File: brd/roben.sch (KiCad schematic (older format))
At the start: 44 parts, among them J1 POWER IN, J10 1+, J11 1-, J12 2-, J13 2+, J2 +V, J3 GND, J4 +V, J5 GND, J6 A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

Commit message: chg: dev: añadidas referencias datasheet y BOM
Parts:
- C1: Vendor (none) -> 81-GRM219R6YA475M3D3
- C2, C4: Vendor (none) -> 843-0805J0500104KJT
- C3: Vendor (none) -> 77-VJ0805Y822KXBPBC
- C5: Vendor (none) -> 77-VJ0805A391KXACBC
- C6: Vendor (none) -> 603-CC805DRNPO9BN7R0
- C7: Vendor (none) -> 81-GRM219R61C226ME5L
- C8: Vendor (none) -> 140-VE101M1CTR0605
- D1, D2, D7: Vendor (none) -> 621-B340-F
- D3, D4, D5, D6: Vendor (none) -> 821-BZT52B5V1
- D8: Vendor (none) -> 720-LOR976-PS-1
- F1: Vendor (none) -> 530-0ZCF0200FF2C
- J1: Vendor (none) -> 651-1985946
- L1: Vendor (none) -> 652-SRN8040-8R2Y
- R10, R6, R7, R8, R9: Vendor (none) -> 71-CRCW0805-220-E3
- R2: Vendor (none) -> 71-CRCW0805-1.0M-E3
- R3: Vendor (none) -> 71-CRCW0805-10K-E3
- R4: Vendor (none) -> 71-CRCW0805-2.0K-E3
- R5: Vendor (none) -> 71-CRCW0805-63.4K-E3
- U1: Vendor (none) -> 595-TPS54232DR
- U2: Vendor (none) -> 595-SN754410NE
- U3: Vendor (none) -> 992-ARD-NANO30
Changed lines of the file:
@@
 F 1 "TPS54232" H 3350 1875 50  0000 C CNN
 F 2 "Housings_SOIC:SOIC-8_3.9x4.9mm_Pitch1.27mm" H 3350 1775 50  0001 C CNN
-F 3 "DOCUMENTATION" H 3350 1775 50  0001 C CNN
+F 3 "http://www.ti.com/lit/ds/symlink/tps54232.pdf" H 3350 1775 50  0001 C CNN
+F 4 "595-TPS54232DR" H 3350 1775 60  0001 C CNN "Vendor"
 	1    3350 1775
 	1    0    0    -1
@@
 F 1 "SN754410N" H 3525 4725 50  0000 C CNN
 F 2 "Housings_DIP:DIP-16__300_ELL" H 3525 4625 50  0001 C CNN
-F 3 "DOCUMENTATION" H 3525 4625 50  0001 C CNN
+F 3 "http://www.ti.com/lit/ds/symlink/sn754410.pdf" H 3525 4625 50  0001 C CNN
+F 4 "595-SN754410NE" H 3525 4625 60  0001 C CNN "Vendor"
 	1    3525 4625
 	1    0    0    -1
@@
 F 2 "asrdi-conn:MKDSN-1985946-02" H 750 1800 60  0001 C CNN
 F 3 "" H 750 1800 60  0000 C CNN
+F 4 "651-1985946" H 750 1800 60  0001 C CNN "Vendor"
 	1    750  1800
 	-1   0    0    1
@@
 F 2 "Diodes_SMD:Diode-SMC_Handsoldering" H 1425 1800 60  0001 C CNN
 F 3 "" H 1425 1800 60  0000 C CNN
+F 4 "621-B340-F" H 1425 1800 60  0001 C CNN "Vendor"
 	1    1425 1800
 	0    1    1    0
@@
 F 2 "Capacitors_SMD:C_0805_HandSoldering" H 3388 1075 30  0001 C CNN
 F 3 "" H 3350 1225 60  0000 C CNN
+F 4 "843-0805J0500104KJT" H 3350 1225 60  0001 C CNN "Vendor"
 	1    3350 1225
 	0    1    1    0
@@
 F 2 "Resistors_SMD:R_0805_HandSoldering" V 2030 2350 30  0001 C CNN
 F 3 "" H 2100 2350 30  0000 C CNN
+F 4 "71-CRCW0805-1.0M-E3" V 2100 2350 60  0001 C CNN "Vendor"
 	1    2100 2350
 	1    0    0    -1
@@
 F 2 "Capacitors_SMD:C_0805_HandSoldering" H 2588 2025 30  0001 C CNN
 F 3 "" H 2550 2175 60  0000 C CNN
+F 4 "77-VJ0805Y822KXBPBC" H 2550 2175 60  0001 C CNN "Vendor"
 	1    2550 2175
 	1    0    0    -1
@@
 F 2 "Capacitors_SMD:C_0805_HandSoldering" H 1813 1775 30  0001 C CNN
 F 3 "" H 1775 1925 60  0000 C CNN
+F 4 "81-GRM219R6YA475M3D3" H 1775 1925 60  0001 C CNN "Vendor"
 	1    1775 1925
 	1    0    0    -1
@@
 F 2 "Capacitors_SMD:C_0805_HandSoldering" H 4813 2325 30  0001 C CNN
 F 3 "" H 4775 2475 60  0000 C CNN
+F 4 "77-VJ0805A391KXACBC" H 4775 2475 60  0001 C CNN "Vendor"
 	1    4775 2475
 	1    0    0    -1
@@
 F 2 "Capacitors_SMD:C_0805_HandSoldering" H 5063 2125 30  0001 C CNN
 F 3 "" H 5025 2275 60  0000 C CNN
+F 4 "603-CC805DRNPO9BN7R0" H 5025 2275 60  0001 C CNN "Vendor"
 	1    5025 2275
 	1    0    0    -1
@@
 F 2 "Resistors_SMD:R_0805_HandSoldering" V 4705 2050 30  0001 C CNN
 F 3 "" H 4775 2050 30  0000 C CNN
+F 4 "71-CRCW0805-63.4K-E3" V 4775 2050 60  0001 C CNN "Vendor"
 	1    4775 2050
 	1    0    0    -1
@@
 F 2 "Resistors_SMD:R_0805_HandSoldering" V 4355 2200 30  0001 C CNN
 F 3 "" H 4425 2200 30  0000 C CNN
+F 4 "71-CRCW0805-2.0K-E3" V 4425 2200 60  0001 C CNN "Vendor"
 	1    4425 2200
 	1    0    0    -1
@@
 F 2 "Resistors_SMD:R_0805_HandSoldering" V 4355 1575 30  0001 C CNN
 F 3 "" H 4425 1575 30  0000 C CNN
+F 4 "71-CRCW0805-10K-E3" V 4425 1575 60  0001 C CNN "Vendor"
 	1    4425 1575
 	1    0    0    -1
@@
 F 2 "Diodes_SMD:Diode-SMC_Handsoldering" H 5225 1500 60  0001 C CNN
 F 3 "" H 5225 1500 60  0000 C CNN
+F 4 "621-B340-F" H 5225 1500 60  0001 C CNN "Vendor"
 	1    5225 1500
 	0    1    1    0
@@
 F 2 "Choke_SMD:Choke_SMD_Wuerth-WE-PD-Typ-M-Typ-S_Handsoldering" H 5650 1225 60  0001 C CNN
 F 3 "" H 5650 1225 60  0000 C CNN
+F 4 "652-SRN8040-8R2Y" V 5650 1225 60  0001 C CNN "Vendor"
 	1    5650 1225
 	0    -1   -1   0
@@
 F 2 "Capacitors_SMD:C_0805_HandSoldering" H 6238 1350 30  0001 C CNN
 F 3 "" H 6200 1500 60  0000 C CNN
+F 4 "81-GRM219R61C226ME5L" H 6200 1500 60  0001 C CNN "Vendor"
 	1    6200 1500
 	1    0    0    -1
@@
 F 2 "Diodes_SMD:Diode-SMC_Handsoldering" H 9875 1900 60  0001 C CNN
 F 3 "" H 9875 1900 60  0000 C CNN
+F 4 "621-B340-F" H 9875 1900 60  0001 C CNN "Vendor"
 	1    9875 1900
 	-1   0    0    1
@@
 F 2 "Resistors_SMD:R_0805_HandSoldering" V 9780 2300 30  0001 C CNN
 F 3 "" H 9850 2300 30  0000 C CNN
+F 4 "71-CRCW0805-220-E3" V 9850 2300 60  0001 C CNN "Vendor"
 	1    9850 2300
 	0    1    1    0
@@
 F 2 "Resistors_SMD:R_0805_HandSoldering" V 9780 2500 30  0001 C CNN
 F 3 "" H 9850 2500 30  0000 C CNN
+F 4 "71-CRCW0805-220-E3" V 9850 2500 60  0001 C CNN "Vendor"
 	1    9850 2500
 	0    1    1    0
@@
 F 2 "Resistors_SMD:R_0805_HandSoldering" V 9480 2400 30  0001 C CNN
 F 3 "" H 9550 2400 30  0000 C CNN
+F 4 "71-CRCW0805-220-E3" V 9550 2400 60  0001 C CNN "Vendor"
 	1    9550 2400
 	0    1    1    0
@@
 F 2 "Resistors_SMD:R_0805_HandSoldering" V 9480 2600 30  0001 C CNN
 F 3 "" H 9550 2600 30  0000 C CNN
+F 4 "71-CRCW0805-220-E3" V 9550 2600 60  0001 C CNN "Vendor"
 	1    9550 2600
 	0    1    1    0
@@
 F 2 "Diodes_SMD:SOD-123" H 9350 3225 60  0001 C CNN
 F 3 "" H 9350 3225 60  0000 C CNN
+F 4 "821-BZT52B5V1" H 9350 3225 60  0001 C CNN "Vendor"
 	1    9350 3225
 	0    1    1    0
@@
 F 2 "Diodes_SMD:SOD-123" H 9075 3225 60  0001 C CNN
 F 3 "" H 9075 3225 60  0000 C CNN
+F 4 "821-BZT52B5V1" H 9075 3225 60  0001 C CNN "Vendor"
 	1    9075 3225
 	0    1    1    0
@@
 F 2 "Diodes_SMD:SOD-123" H 8800 3225 60  0001 C CNN
 F 3 "" H 8800 3225 60  0000 C CNN
+F 4 "821-BZT52B5V1" H 8800 3225 60  0001 C CNN "Vendor"
 	1    8800 3225
 	0    1    1    0
@@
 F 2 "Diodes_SMD:SOD-123" H 8525 3225 60  0001 C CNN
 F 3 "" H 8525 3225 60  0000 C CNN
+F 4 "821-BZT52B5V1" H 8525 3225 60  0001 C CNN "Vendor"
 	1    8525 3225
 	0    1    1    0
@@
 F 2 "Housings_DIP:DIP-32__600_ELL" H 6200 4225 50  0001 C CNN
 F 3 "DOCUMENTATION" H 6200 4225 50  0001 C CNN
+F 4 "992-ARD-NANO30" H 6200 4225 60  0001 C CNN "Vendor"
 	1    6200 4225
 	1    0    0    -1
@@
 F 2 "Capacitors_SMD:C_0805_HandSoldering" H 1888 4500 30  0001 C CNN
 F 3 "" H 1850 4650 60  0000 C CNN
+F 4 "843-0805J0500104KJT" H 1850 4650 60  0001 C CNN "Vendor"
 	1    1850 4650
 	1    0    0    -1
@@
 F 2 "Capacitors_SMD:c_elec_6.3x5.3" H 6538 1350 30  0001 C CNN
 F 3 "" H 6500 1500 60  0000 C CNN
+F 4 "140-VE101M1CTR0605" H 6500 1500 60  0001 C CNN "Vendor"
 	1    6500 1500
 	1    0    0    -1
@@
 F 2 "Fuse_Holders_and_Fuses:Fuse_SMD2920" H 1175 1625 60  0001 C CNN
 F 3 "" H 1175 1625 60  0000 C CNN
+F 4 "530-0ZCF0200FF2C" H 1175 1625 60  0001 C CNN "Vendor"
 	1    1175 1625
 	1    0    0    -1
@@
 F 2 "Resistors_SMD:R_0805_HandSoldering" V 6755 1500 30  0001 C CNN
 F 3 "" H 6825 1500 30  0000 C CNN
+F 4 "71-CRCW0805-220-E3" V 6825 1500 60  0001 C CNN "Vendor"
 	1    6825 1500
 	1    0    0    -1
@@
 F 2 "LEDs:LED-0805" H 6825 1950 60  0001 C CNN
 F 3 "" H 6825 1950 60  0000 C CNN
+F 4 "720-LOR976-PS-1" H 6825 1950 60  0001 C CNN "Vendor"
 	1    6825 1950
 	0    -1   -1   0

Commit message: new: modificada inversión de polaridad según #1
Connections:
- wire segments 157 -> 179
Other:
- moved on the sheet: D1, F1
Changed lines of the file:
@@
 L D D1
 U 1 1 55BBE048
-P 1425 1800
-F 0 "D1" H 1425 1900 50  0000 C CNN
-F 1 "B340" H 1425 1700 50  0000 C CNN
-F 2 "Diodes_SMD:Diode-SMC_Handsoldering" H 1425 1800 60  0001 C CNN
-F 3 "" H 1425 1800 60  0000 C CNN
-F 4 "621-B340-F" H 1425 1800 60  0001 C CNN "Vendor"
-	1    1425 1800
-	0    1    1    0
+P 1175 1625
+F 0 "D1" H 1175 1725 50  0000 C CNN
+F 1 "B340" H 1175 1525 50  0000 C CNN
+F 2 "Diodes_SMD:Diode-SMC_Handsoldering" H 1175 1625 60  0001 C CNN
+F 3 "" H 1175 1625 60  0000 C CNN
+F 4 "621-B340-F" H 1175 1625 60  0001 C CNN "Vendor"
+	1    1175 1625
+	-1   0    0    1
 $EndComp
 $Comp
 L GND #PWR01
 U 1 1 55BBE1AF
-P 1425 2050
-F 0 "#PWR01" H 1425 1800 50  0001 C CNN
-F 1 "GND" H 1425 1900 50  0000 C CNN
-F 2 "" H 1425 2050 60  0000 C CNN
-F 3 "" H 1425 2050 60  0000 C CNN
-	1    1425 2050
+P 975 1975
+F 0 "#PWR01" H 975 1725 50  0001 C CNN
+F 1 "GND" H 975 1825 50  0000 C CNN
+F 2 "" H 975 1975 60  0000 C CNN
+F 3 "" H 975 1975 60  0000 C CNN
+	1    975  1975
 	1    0    0    -1
 $EndComp
@@
 	975  1750 975  1625
 Wire Wire Line
-	975  1625 1075 1625
-Wire Wire Line
-	1275 1625 1625 1625
-Wire Wire Line
-	1425 1625 1425 1650
+	975  1625 1025 1625
 Wire Wire Line
 	950  1850 975  1850
 Wire Wire Line
-	975  1850 975  2000
-Wire Wire Line
-	975  2000 1425 2000
-Wire Wire Line
-	1425 1950 1425 2050
-Connection ~ 1425 2000
-Wire Wire Line
-	1625 1725 2600 1725
+	975  1850 975  1975
+Wire Wire Line
+	1625 1725 1775 1725
+Wire Wire Line
+	1775 1725 2100 1725
+Wire Wire Line
+	2100 1725 2600 1725
 Wire Wire Line
 	1625 1625 1625 1725
-Connection ~ 1425 1625
 Wire Wire Line
 	2600 1625 2525 1625
@@
 	2525 1225 3200 1225
 Wire Wire Line
-	3500 1225 5350 1225
+	3500 1225 4225 1225
+Wire Wire Line
+	4225 1225 5225 1225
+Wire Wire Line
+	5225 1225 5350 1225
 Wire Wire Line
 	4225 1225 4225 1625
@@
 	2100 2600 2100 2500
 Wire Wire Line
-	2100 2075 2100 2200
+	2100 2075 2100 2125
+Wire Wire Line
+	2100 2125 2100 2200
 Wire Wire Line
 	2100 1775 2100 1725
@@
 $EndComp
 Wire Wire Line
-	4100 1825 5025 1825
+	4100 1825 4775 1825
+Wire Wire Line
+	4775 1825 5025 1825
 Wire Wire Line
 	4775 1825 4775 1900
@@
 	4775 2625 4775 2700
 Wire Wire Line
-	4775 2700 5025 2700
+	4775 2700 4900 2700
+Wire Wire Line
+	4900 2700 5025 2700
 Wire Wire Line
 	4900 2700 4900 2775
@@
 	4100 1925 4425 1925
 Wire Wire Line
-	4425 1725 4425 2050
+	4425 1725 4425 1925
+Wire Wire Line
+	4425 1925 4425 2050
 Connection ~ 4425 1925
 $Comp
@@
 Connection ~ 5225 1225
 Wire Wire Line
-	5950 1225 6825 1225
-Wire Wire Line
-	6200 775  6200 1350
+	5950 1225 6200 1225
+Wire Wire Line
+	6200 1225 6500 1225
+Wire Wire Line
+	6500 1225 6825 1225
+Wire Wire Line
+	6200 775  6200 850
+Wire Wire Line
+	6200 850  6200 1225
+Wire Wire Line
+	6200 1225 6200 1350
 Wire Wire Line
 	4425 1425 4425 850
@@
 $EndComp
 Wire Wire Line
-	10200 2000 10200 3150
+	10200 2000 10200 2200
+Wire Wire Line
+	10200 2200 10200 3150
 Wire Wire Line
 	10200 2000 10300 2000
@@
 	10125 2100 10125 1900
 Wire Wire Line
-	10025 1900 10300 1900
+	10025 1900 10125 1900
+Wire Wire Line
+	10125 1900 10300 1900
 Connection ~ 10125 1900
 Wire Wire Line
@@
 	9350 3025 9350 2600
 Wire Wire Line
-	8200 2600 9400 2600
+	8200 2600 9350 2600
+Wire Wire Line
+	9350 2600 9400 2600
 Wire Wire Line
 	9075 3025 9075 2500
 Wire Wire Line
-	8025 2500 9700 2500
+	8025 2500 9075 2500
+Wire Wire Line
+	9075 2500 9700 2500
 Wire Wire Line
 	8800 3025 8800 2400
 Wire Wire Line
-	7825 2400 9400 2400
+	7825 2400 8800 2400
+Wire Wire Line
+	8800 2400 9400 2400
 Wire Wire Line
 	8525 3025 8525 2300
 Wire Wire Line
-	7600 2300 9700 2300
+	7600 2300 8525 2300
+Wire Wire Line
+	8525 2300 9700 2300
 $Comp
 L GND #PWR013
@@
 	7600 4425 6950 4425
 Wire Wire Line
-	7600 2300 7600 4425
+	7600 2300 7600 3125
+Wire Wire Line
+	7600 3125 7600 4425
 Connection ~ 8525 2300
 Wire Wire Line
@@
 	7825 4325 6950 4325
 Wire Wire Line
-	7825 2400 7825 4325
+	7825 2400 7825 2975
+Wire Wire Line
+	7825 2975 7825 4325
 Connection ~ 8800 2400
 Wire Wire Line
@@
 	6950 4125 8025 4125
 Wire Wire Line
-	8025 2500 8025 4925
+	8025 2500 8025 4125
+Wire Wire Line
+	8025 4125 8025 4925
 Connection ~ 9075 2500
 Wire Wire Line
 	6950 4225 8200 4225
 Wire Wire Line
-	8200 2600 8200 5300
+	8200 2600 8200 4225
+Wire Wire Line
+	8200 4225 8200 5300
 Connection ~ 9350 2600
 $Comp
@@
 	4275 4575 4350 4575
 Wire Wire Line
-	4350 4575 4350 5200
+	4350 4575 4350 4675
+Wire Wire Line
+	4350 4675 4350 5200
 Wire Wire Line
 	4275 4675 4350 4675
@@
 	2775 4575 2675 4575
 Wire Wire Line
-	2675 4575 2675 5200
+	2675 4575 2675 4675
+Wire Wire Line
+	2675 4675 2675 5200
 Wire Wire Line
 	2775 4675 2675 4675
@@
 L F_Small F1
 U 1 1 55BC97BC
-P 1175 1625
-F 0 "F1" H 1135 1685 50  0000 L CNN
-F 1 "2A PPTC" H 1055 1565 50  0000 L CNN
-F 2 "Fuse_Holders_and_Fuses:Fuse_SMD2920" H 1175 1625 60  0001 C CNN
-F 3 "" H 1175 1625 60  0000 C CNN
-F 4 "530-0ZCF0200FF2C" H 1175 1625 60  0001 C CNN "Vendor"
-	1    1175 1625
+P 1475 1625
+F 0 "F1" H 1435 1685 50  0000 L CNN
+F 1 "2A PPTC" H 1355 1565 50  0000 L CNN
+F 2 "Fuse_Holders_and_Fuses:Fuse_SMD2920" H 1475 1625 60  0001 C CNN
+F 3 "" H 1475 1625 60  0000 C CNN
+F 4 "530-0ZCF0200FF2C" H 1475 1625 60  0001 C CNN "Vendor"
+	1    1475 1625
 	1    0    0    -1
 $EndComp
@@
 	8025 4925 6950 4925
 Connection ~ 8025 4125
+Wire Wire Line
+	1325 1625 1375 1625
+Wire Wire Line
+	1625 1625 1575 1625
 $EndSCHEMATC

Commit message: new: reemplazado step-down por sepic, segun #2
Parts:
- removed C1: 4.7uF, Capacitors_SMD:C_0805_HandSoldering, symbol C
- removed C3: 8.2nF, Capacitors_SMD:C_0805_HandSoldering, symbol C
- removed C4: 100nF, Capacitors_SMD:C_0805_HandSoldering, symbol C
- removed C5: 390pF, Capacitors_SMD:C_0805_HandSoldering, symbol C
- removed C6: 7pF, Capacitors_SMD:C_0805_HandSoldering, symbol C
- removed C7: 22uF, Capacitors_SMD:C_0805_HandSoldering, symbol C
- removed C8: 100uF, Capacitors_SMD:c_elec_6.3x5.3, symbol CP
- removed D2: B340, Diodes_SMD:Diode-SMC_Handsoldering, symbol D_Schottky
- removed L1: 8.2uH, Choke_SMD:Choke_SMD_Wuerth-WE-PD-Typ-M-Typ-S_Handsoldering, symbol INDUCTOR
- removed R1, R3: 10k, Resistors_SMD:R_0805_HandSoldering, symbol R
- removed R2: 1M, Resistors_SMD:R_0805_HandSoldering, symbol R
- removed R4: 2k, Resistors_SMD:R_0805_HandSoldering, symbol R
- removed R5: 63.4k, Resistors_SMD:R_0805_HandSoldering, symbol R
- removed U1: TPS54232, Housings_SOIC:SOIC-8_3.9x4.9mm_Pitch1.27mm, symbol TPS54232
- added C? (x2): 100nF, symbol C
- added C?: 2.4nF, symbol C
- added C?: 4.7uF, symbol C
- added C?: 1.2nF, symbol C
- added C?: 5.6uF, symbol CP
- added C?: 330uF, symbol CP
- added D?: B540, symbol D
- added L?: 33uH, symbol INDUCTOR
- added L?: 10uH, symbol INDUCTOR
- added Q?: DMN6068LK3-13, symbol Q_NMOS_GDS
- added R?: 20R, symbol R
- added R?: 1k58, symbol R
- added R?: 29k4, symbol R
- added R?: 10k, symbol R
- added R?: 63k4, symbol R
- added R?: 18m, symbol R
- added R?: 100R, symbol R
- added U?: LM3488, MODULE, symbol LM3488
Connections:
- wire segments 179 -> 163
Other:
- moved on the sheet: C2, D1, D3, D4, D5, D6, D7, D8, F1, J1, J10, J11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

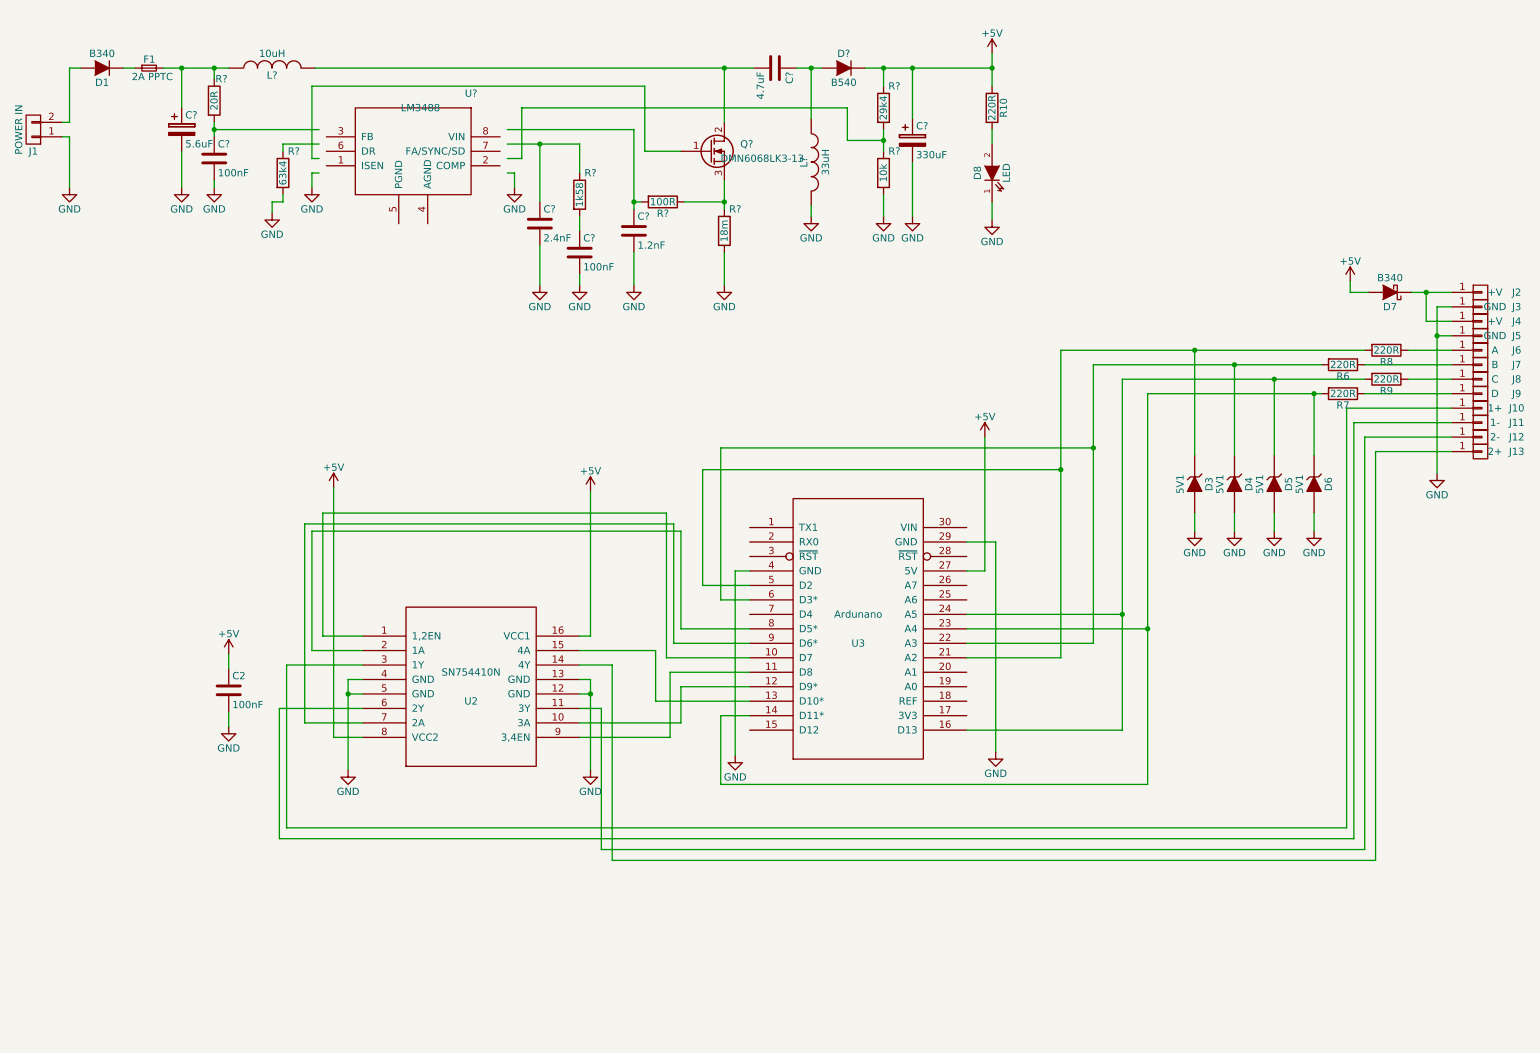
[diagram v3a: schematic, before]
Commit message: new: añadidos periféricos en pines libres, segun #4
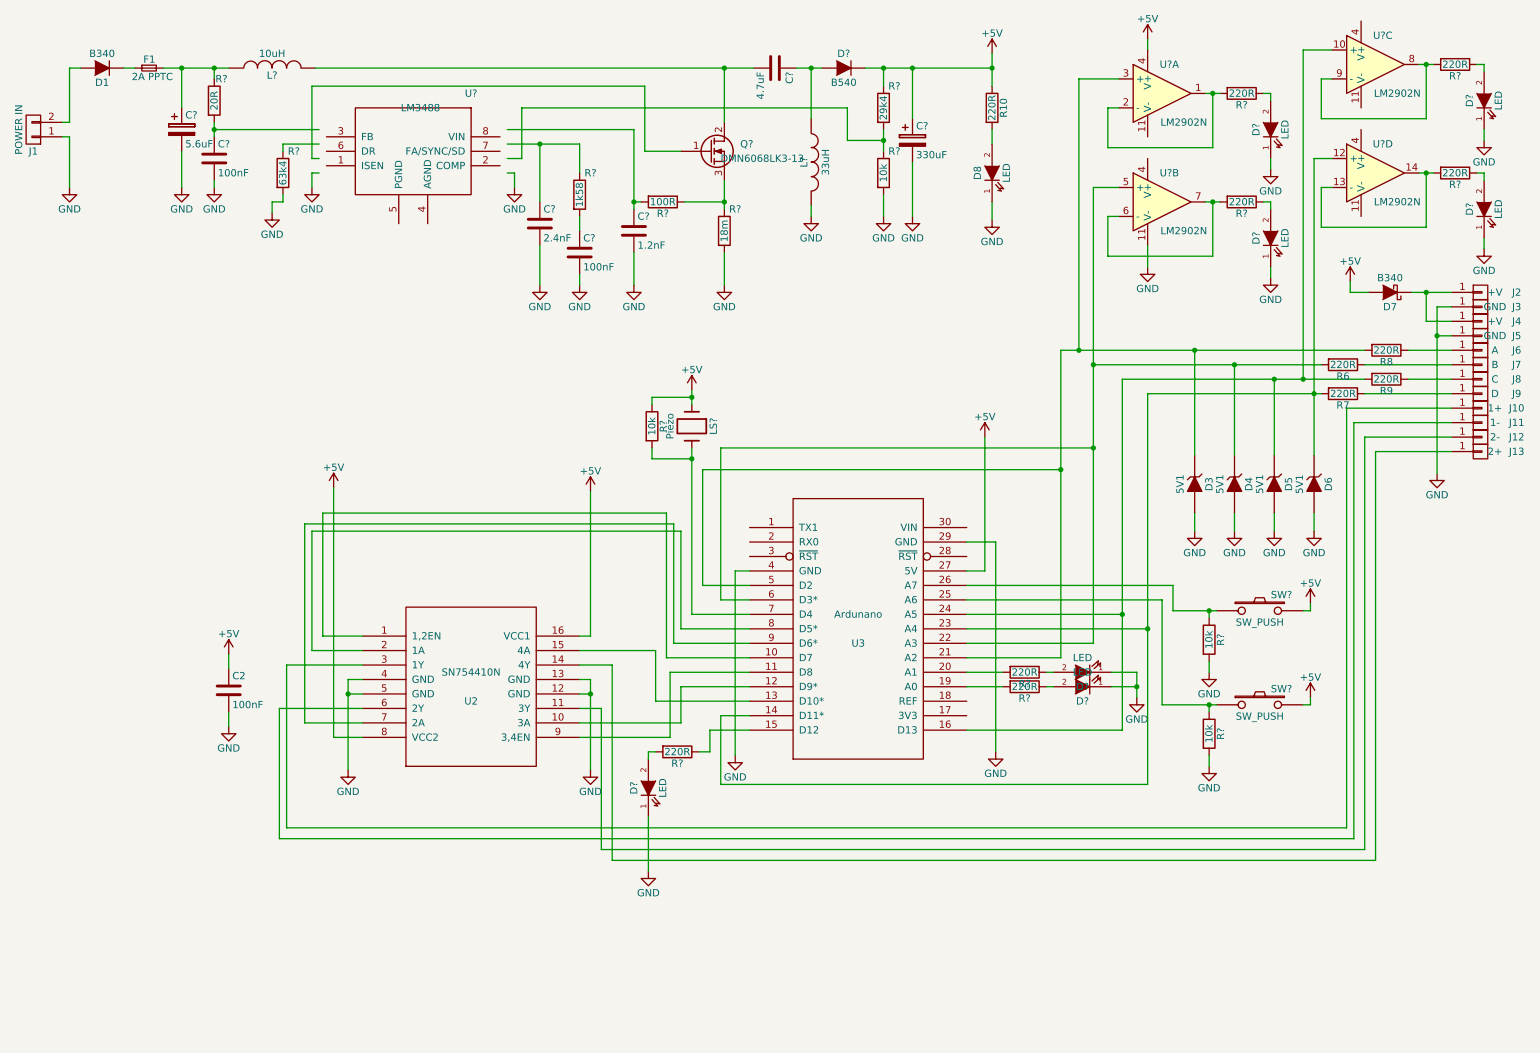
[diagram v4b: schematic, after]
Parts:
- added D? (x7): LED, LEDs:LED-0805, symbol LED
- added LS?: Piezo, symbol Crystal
- added R? (x7): 220R, Resistors_SMD:R_0805_HandSoldering, symbol R
- added R? (x3): 10k, symbol R
- added SW? (x2): SW_PUSH, symbol SW_PUSH
- added U? (x4): LM2902N, symbol LM2902N
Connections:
- wire segments 163 -> 237
